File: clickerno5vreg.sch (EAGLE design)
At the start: 50 parts, among them IC1 DW01A, IC2 TP4056, J1 DX07S016JA1R1500, Q1 FS8205A, U1 TPS61040DBVR, Y1 16MHz

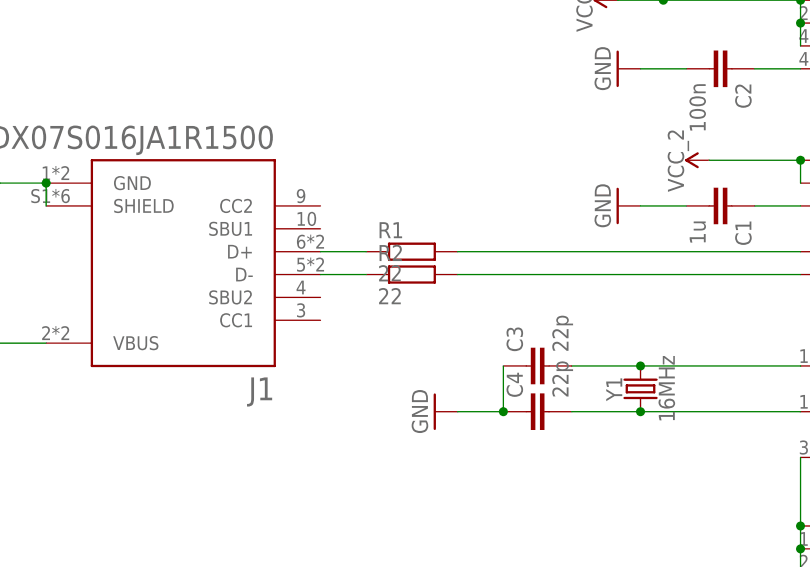
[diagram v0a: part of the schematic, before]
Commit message: added pd resistors
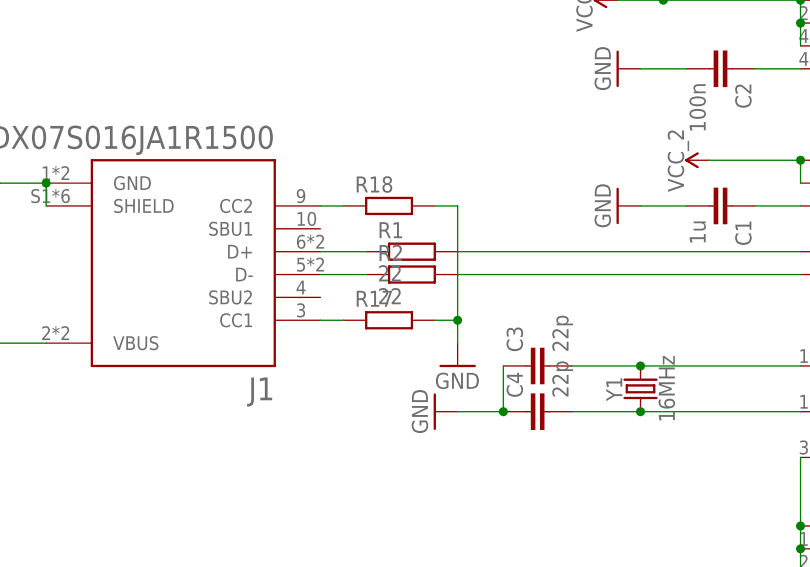
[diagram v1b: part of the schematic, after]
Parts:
- added R17, R18: (no value), rcl:R-EU_R0603
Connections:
- new net N$31: J1.CC1, R17.1
- new net N$32: J1.CC2, R18.1
- net GND: now also R17.2, R18.2
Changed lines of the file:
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@@
 <part name="PAD3" library="wirepad" library_urn="urn:adsk.eagle:library:412" deviceset="SMD5" device="" package3d_urn="urn:adsk.eagle:package:30841/1"/>
 <part name="PAD4" library="wirepad" library_urn="urn:adsk.eagle:library:412" deviceset="SMD5" device="" package3d_urn="urn:adsk.eagle:package:30841/1"/>
+<part name="R17" library="rcl" library_urn="urn:adsk.eagle:library:334" deviceset="R-EU_" device="R0603" package3d_urn="urn:adsk.eagle:package:23555/3"/>
+<part name="R18" library="rcl" library_urn="urn:adsk.eagle:library:334" deviceset="R-EU_" device="R0603" package3d_urn="urn:adsk.eagle:package:23555/3"/>
+<part name="GND12" library="supply1" library_urn="urn:adsk.eagle:library:371" deviceset="GND" device=""/>
 </parts>
 <sheets>
@@
 <attribute name="NAME" x="77.597" y="22.1742" size="1.778" layer="95"/>
 <attribute name="VALUE" x="77.597" y="17.018" size="1.778" layer="96"/>
+</instance>
+<instance part="R17" gate="G$1" x="43.18" y="60.96" smashed="yes">
+<attribute name="NAME" x="39.37" y="62.4586" size="1.778" layer="95"/>
+<attribute name="VALUE" x="39.37" y="57.658" size="1.778" layer="96"/>
+</instance>
+<instance part="R18" gate="G$1" x="43.18" y="73.66" smashed="yes">
+<attribute name="NAME" x="39.37" y="75.1586" size="1.778" layer="95"/>
+<attribute name="VALUE" x="39.37" y="70.358" size="1.778" layer="96"/>
+</instance>
+<instance part="GND12" gate="1" x="50.8" y="55.88" smashed="yes">
+<attribute name="VALUE" x="48.26" y="53.34" size="1.778" layer="96"/>
 </instance>
 </instances>
@@
 <wire x1="269.24" y1="147.32" x2="269.24" y2="142.24" width="0.1524" layer="91"/>
 </segment>
+<segment>
+<pinref part="R18" gate="G$1" pin="2"/>
+<pinref part="GND12" gate="1" pin="GND"/>
+<wire x1="48.26" y1="73.66" x2="50.8" y2="73.66" width="0.1524" layer="91"/>
+<wire x1="50.8" y1="73.66" x2="50.8" y2="60.96" width="0.1524" layer="91"/>
+<pinref part="R17" gate="G$1" pin="2"/>
+<wire x1="50.8" y1="60.96" x2="50.8" y2="58.42" width="0.1524" layer="91"/>
+<wire x1="48.26" y1="60.96" x2="50.8" y2="60.96" width="0.1524" layer="91"/>
+<junction x="50.8" y="60.96"/>
+</segment>
 </net>
 <net name="N$1" class="0">
@@
 </segment>
 </net>
+<net name="N$31" class="0">
+<segment>
+<pinref part="J1" gate="G$1" pin="CC1"/>
+<pinref part="R17" gate="G$1" pin="1"/>
+<wire x1="35.56" y1="60.96" x2="38.1" y2="60.96" width="0.1524" layer="91"/>
+</segment>
+</net>
+<net name="N$32" class="0">
+<segment>
+<pinref part="J1" gate="G$1" pin="CC2"/>
+<pinref part="R18" gate="G$1" pin="1"/>
+<wire x1="35.56" y1="73.66" x2="38.1" y2="73.66" width="0.1524" layer="91"/>
+</segment>
+</net>
